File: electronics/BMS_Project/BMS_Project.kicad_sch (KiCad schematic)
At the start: 0 parts

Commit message: Meeting 28.04.2023 worked on schematic
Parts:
- added J1: Conn_01x20_Pin, symbol Connector:Conn_01x20_Pin
- added PAD1, PAD2: Prototyping_Pad_Data, BMS_lib:Prototyping_Pad_Data, symbol BMS_lib:Prototyping_Pad_Data
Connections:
- new net: J1.17 (Pin_17), PAD1.1
- new net: J1.18 (Pin_18), PAD2.1
- new net +5V: J1.2 (Pin_2)
- new net +BATT: J1.1 (Pin_1)
- new net GND: J1.19 (Pin_19), J1.20 (Pin_20)
- new net balancing_ctrl_1: J1.3 (Pin_3)
- new net balancing_ctrl_2: J1.4 (Pin_4)
- new net balancing_ctrl_3: J1.5 (Pin_5)
- new net balancing_ctrl_4: J1.6 (Pin_6)
- new net bat01: J1.7 (Pin_7)
- new net bat02: J1.8 (Pin_8)
- new net bat03: J1.9 (Pin_9)
- new net bat04: J1.10 (Pin_10)
- new net bat_main_switch: J1.15 (Pin_15)
- new net current_sensor: J1.16 (Pin_16)
- new net temp_sensor01: J1.11 (Pin_11)
- new net temp_sensor02: J1.12 (Pin_12)
- new net temp_sensor03: J1.13 (Pin_13)
- new net temp_sensor04: J1.14 (Pin_14)
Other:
- removed sheet Balancing
- sheet Arduino ports: added CAN_MISO, CAN_MOSI, CAN_SCK, balance_status_1, balance_status_2, balance_status_3, balance_status_4, bat_main_switch, cell_1_V, cell_2_V, cell_3_V, cell_4_V, current, temp_1, temp_2, temp_3, temp_4; removed none
- sheet Temp_sensor_circuit ports: added Temp_1, Temp_2, Temp_3, Temp_4, sensor_1, sensor_2, sensor_3, sensor_4; removed none
- sheet U_Messung ports: added BT1_+/BT2_-, BT2_+/BT3_-, BT3_+/BT4_-, BT4_+; removed BT1_+, BT1_-/BT2_+, BT2_-/BT3_+, BT3_-/BT4_+
- note removed: "Fabi"
- note removed: "John werte/values"
- note removed: "Michi"

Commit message: discord session with Johannes and Fabian, Schematic nearly done, all footprints fields filled
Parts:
- added F1: Fuse, Fuse:Fuse_1206_3216Metric, symbol Device:Fuse
- added J2, J6: Conn_01x01_Socket, Connector:Banana_Jack_1Pin, symbol Connector:Conn_01x01_Socket
- added J4: ESP32_power, TerminalBlock:TerminalBlock_bornier-2_P5.08mm, symbol Connector:Screw_Terminal_01x02
- added J5: Display_power, TerminalBlock:TerminalBlock_bornier-2_P5.08mm, symbol Connector:Screw_Terminal_01x02
- added Q1: Q_PMOS_GSD, Package_TO_SOT_SMD:SOT-23, symbol Device:Q_PMOS_GSD
- added SW2: SW_SPDT, Button_Switch_THT:SW_Slide_1P2T_CK_OS102011MS2Q, symbol Switch:SW_SPDT
- added U3: Buck, BMS_lib:Buck_LM2596, symbol BMS_lib:Buck_LM2596
- added U4: ~, BMS_lib:CAN_Board, symbol BMS_lib:CAN_board
- J1: footprint (none) -> Connector_IDC:IDC-Header_2x10_P2.54mm_Vertical
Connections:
- net +5V: now also F1.2, J4.1 (Pin_1), Q1.3 (D), U4.7 (VCC)
- net +BATT: now also SW2.3 (C)
- net GND: now also J2.1 (Pin_1), J4.2 (Pin_2), J5.2 (Pin_2), U3.2 (IN-), U3.4 (OUT-), U4.6 (GND)
- new net: SW2.2 (B), U3.1 (IN+)
- new net: F1.1, U3.3 (OUT+)
- new net: J5.1 (Pin_1), Q1.2 (S)
- new net: J6.1 (Pin_1), SW2.1 (A)
- new net CAN_SCK: U4.2 (SCK)
- new net CAN_SI: U4.3 (SI)
- new net CAN_SO: U4.4 (SO)
- new net display_enable: Q1.1 (G)
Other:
- sheet Arduino ports: added Display_enable; removed none
- note added: "?"
- note added: "Done: switch for power - via dcdc converter -> batt - via dcdc converter -> lab power supply one CAN module mosfet switch for display a few small buttons x4 fuse for logic voltage 5V output for ESP32 (mosfet switch -> no) banana sockets for aux power supply TODO: can pins ESP32 location?"
- moved on the sheet: J1, PAD1, PAD2

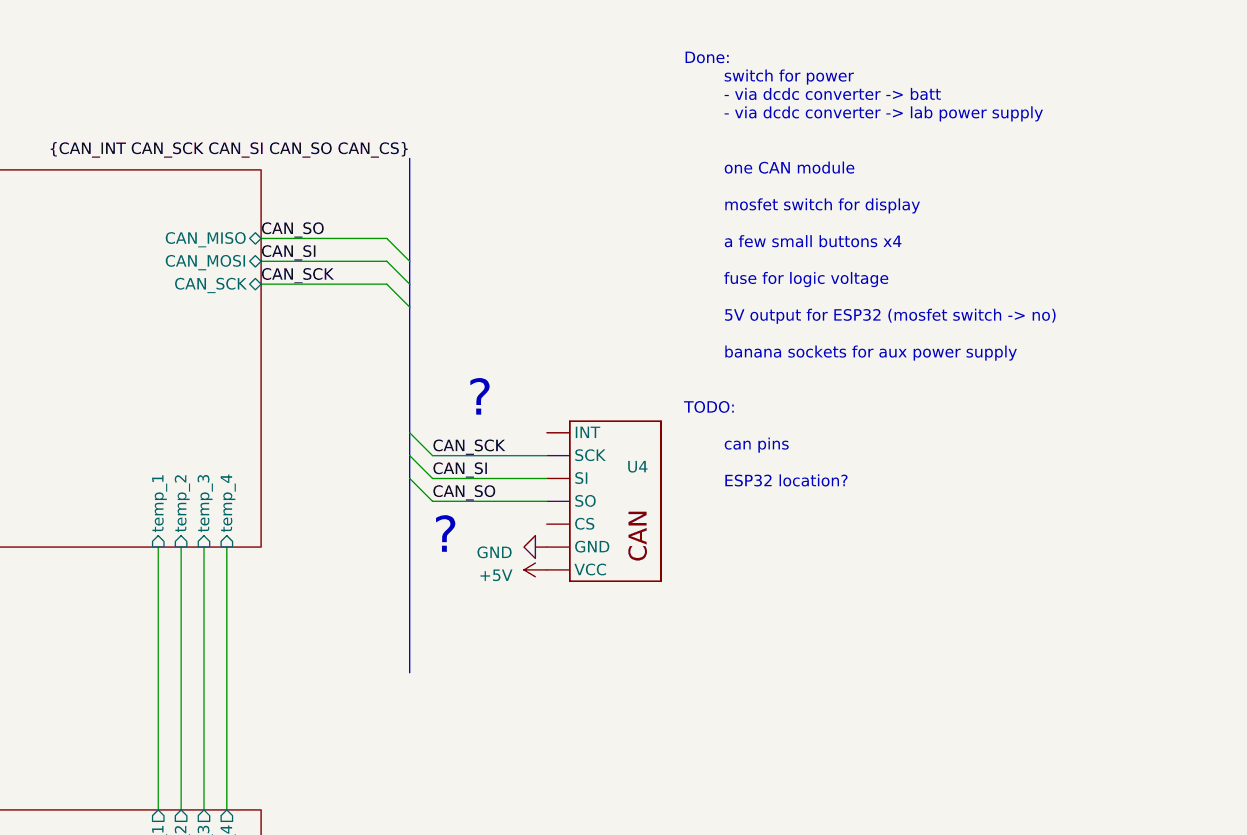
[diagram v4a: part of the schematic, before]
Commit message: schematic done, starting with layout
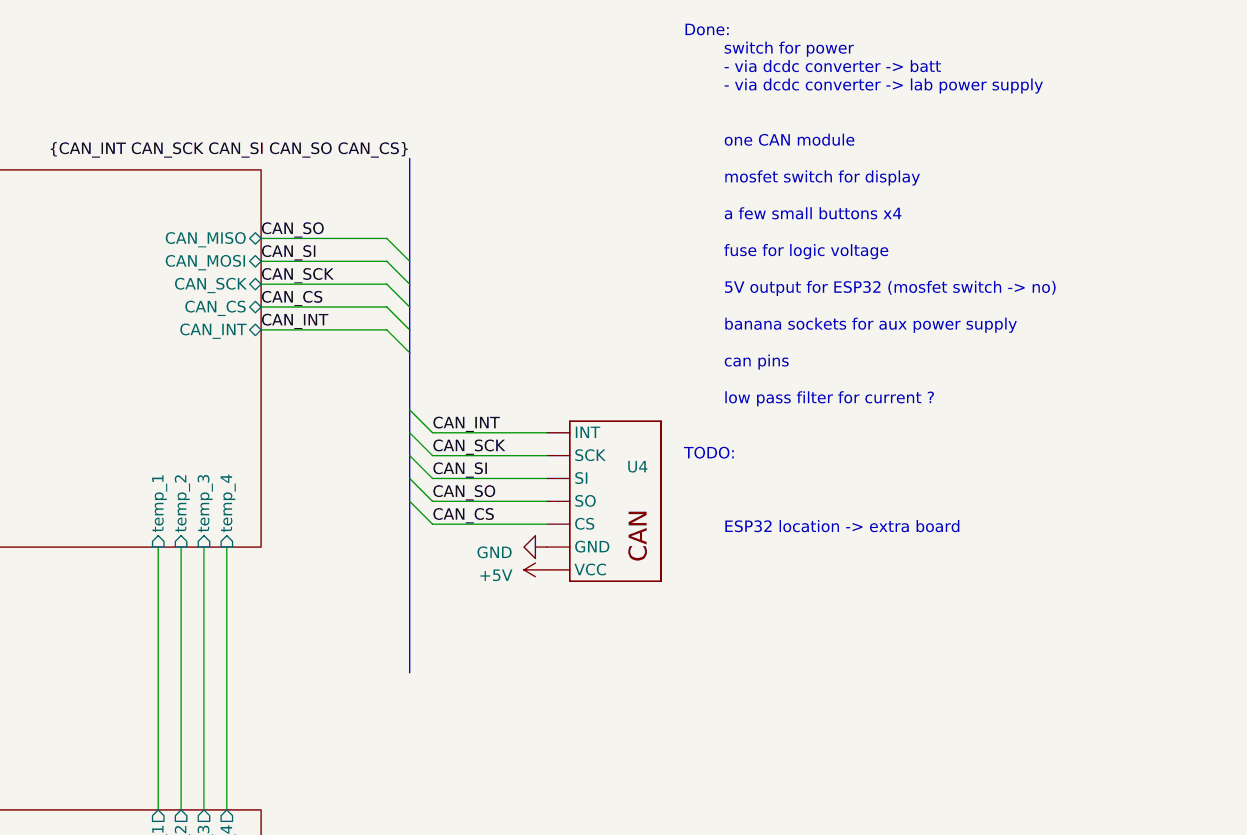
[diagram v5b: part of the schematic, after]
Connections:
- net CAN_INT: now reaches U4.1 (INT)
- net CAN_CS: now reaches U4.5 (CS)
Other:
- sheet Arduino ports: added CAN_CS, CAN_INT; removed none
- note added: "Done: switch for power - via dcdc converter -> batt - via dcdc converter -> lab power supply one CAN module mosfet switch for display a few small buttons x4 fuse for logic voltage 5V output for ESP32 (mosfet switch -> no) banana sockets for aux power supply can pins low pass filter for current ? TODO: ESP32 location -> extra board"
- note removed: "?"
- note removed: "Done: switch for power - via dcdc converter -> batt - via dcdc converter -> lab power supply one CAN module mosfet switch for display a few small buttons x4 fuse for logic voltage 5V output for ESP32 (mosfet switch -> no) banana sockets for aux power supply TODO: can pins ESP32 location?"
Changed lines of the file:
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@@
+    (stroke (width 0) (type default))
+  )
+  (bus_entry (at 201.93 45.72) (size -2.54 -2.54)
     (stroke (width 0) (type default))
   )
@@
     (stroke (width 0) (type default))
   )
+  (bus_entry (at 201.93 48.26) (size -2.54 -2.54)
+    (stroke (width 0) (type default))
+  )
   (bus_entry (at 114.3 115.57) (size 2.54 -2.54)
     (stroke (width 0) (type default))
   )
+  (bus_entry (at 201.93 54.61) (size 2.54 2.54)
+    (stroke (width 0) (type default))
+  )
   (bus_entry (at 114.3 53.34) (size 2.54 -2.54)
     (stroke (width 0) (type default))
@@
     (stroke (width 0) (type default))
   )
+  (bus_entry (at 201.93 64.77) (size 2.54 2.54)
+    (stroke (width 0) (type default))
+  )
   (bus_entry (at 114.3 113.03) (size 2.54 -2.54)
     (stroke (width 0) (type default))
@@
     (stroke (width 0) (type default))
   )
+  (wire (pts (xy 204.47 67.31) (xy 217.17 67.31))
+    (stroke (width 0) (type default))
+  )
   (wire (pts (xy 116.84 53.34) (xy 134.62 53.34))
     (stroke (width 0) (type default))
@@
     (stroke (width 0) (type default))
   )
-  (bus (pts (xy 201.93 43.18) (xy 201.93 57.15))
+  (bus (pts (xy 201.93 43.18) (xy 201.93 45.72))
     (stroke (width 0) (type default))
   )
@@
     (stroke (width 0) (type default))
   )
+  (bus (pts (xy 201.93 54.61) (xy 201.93 57.15))
+    (stroke (width 0) (type default))
+  )
+  (bus (pts (xy 201.93 48.26) (xy 201.93 54.61))
+    (stroke (width 0) (type default))
+  )
   (wire (pts (xy 57.15 180.34) (xy 57.15 181.61))
     (stroke (width 0) (type default))
@@
     (stroke (width 0) (type default))
   )
+  (bus (pts (xy 201.93 45.72) (xy 201.93 48.26))
+    (stroke (width 0) (type default))
+  )
   (bus (pts (xy 201.93 26.67) (xy 201.93 38.1))
     (stroke (width 0) (type default))
@@
     (stroke (width 0) (type default))
   )
-  (bus (pts (xy 201.93 62.23) (xy 201.93 83.82))
+  (bus (pts (xy 201.93 62.23) (xy 201.93 64.77))
+    (stroke (width 0) (type default))
+  )
+  (wire (pts (xy 204.47 57.15) (xy 217.17 57.15))
     (stroke (width 0) (type default))
   )
@@
     (stroke (width 0) (type default))
   )
+  (bus (pts (xy 201.93 64.77) (xy 201.93 83.82))
+    (stroke (width 0) (type default))
+  )
   (wire (pts (xy 30.48 123.19) (xy 50.8 123.19))
     (stroke (width 0) (type default))
@@
     (stroke (width 0) (type default))
   )
+  (wire (pts (xy 185.42 45.72) (xy 199.39 45.72))
+    (stroke (width 0) (type default))
+  )
   (wire (pts (xy 77.47 35.56) (xy 134.62 35.56))
     (stroke (width 0) (type default))
@@
     (stroke (width 0) (type default))
   )
+  (wire (pts (xy 185.42 43.18) (xy 199.39 43.18))
+    (stroke (width 0) (type default))
+  )
   (bus (pts (xy 53.34 120.65) (xy 53.34 123.19))
     (stroke (width 0) (type default))
@@
     (stroke (width 0) (type default))
   )
-  (text "Done:\n		switch for power\n		- via dcdc converter -> batt\n		- via dcdc converter -> lab power supply\n\n\n		one CAN module\n\n		mosfet switch for display\n\n		a few small buttons x4\n\n		fuse for logic voltage\n\n		5V output for ESP32 (mosfet switch -> no)\n\n		banana sockets for aux power supply\n\n\nTODO:\n\n		can pins\n\n		ESP32 location?"
-    (at 232.41 63.5 0)
+  (text "Done:\n		switch for power\n		- via dcdc converter -> batt\n		- via dcdc converter -> lab power supply\n\n\n		one CAN module\n\n		mosfet switch for display\n\n		a few small buttons x4\n\n		fuse for logic voltage\n\n		5V output for ESP32 (mosfet switch -> no)\n\n		banana sockets for aux power supply\n\n		can pins\n\n		low pass filter for current ?\n\n\nTODO:\n\n\n\n		ESP32 location -> extra board\n"
+    (at 232.41 68.58 0)
     (effects (font (size 1.27 1.27)) (justify left bottom))
   )
   (text "GND and +12V\nvia global labels" (at 60.96 25.4 0)
     (effects (font (size 1.27 1.27)) (justify left bottom))
-  )
-  (text "?" (at 208.28 55.88 0)
-    (effects (font (size 4 4)) (justify left bottom))
-  )
-  (text "?" (at 204.47 71.12 0)
-    (effects (font (size 4 4)) (justify left bottom))
   )
   (label "bat_main_switch" (at 30.48 128.27 0) (fields_autoplaced)
@@
     (effects (font (size 1.27 1.27)) (justify left bottom))
   )
+  (label "CAN_CS" (at 185.42 43.18 0)
+    (effects (font (size 1.27 1.27)) (justify left bottom))
+  )
   (label "bat03" (at 30.48 113.03 0) (fields_autoplaced)
     (effects (font (size 1.27 1.27)) (justify left bottom))
@@
     (effects (font (size 1.27 1.27)) (justify left bottom))
   )
+  (label "CAN_INT" (at 204.47 57.15 0)
+    (effects (font (size 1.27 1.27)) (justify left bottom))
+  )
   (label "temp_sensor02" (at 116.84 110.49 0) (fields_autoplaced)
     (effects (font (size 1.27 1.27)) (justify left bottom))
@@
   )
   (label "CAN_SI" (at 185.42 38.1 0) (fields_autoplaced)
+    (effects (font (size 1.27 1.27)) (justify left bottom))
+  )
+  (label "CAN_CS" (at 204.47 67.31 0)
+    (effects (font (size 1.27 1.27)) (justify left bottom))
+  )
+  (label "CAN_INT" (at 185.42 45.72 0)
     (effects (font (size 1.27 1.27)) (justify left bottom))
   )
@@
       (effects (font (size 1.27 1.27)) (justify left))
     )
-    (instances
+    (pin "CAN_CS" bidirectional (at 185.42 43.18 0)
+      (effects (font (size 1.27 1.27)) (justify right))
+    )
+    (pin "CAN_INT" bidirectional (at 185.42 45.72 0)
+      (effects (font (size 1.27 1.27)) (justify right))
+    )
+    (instances

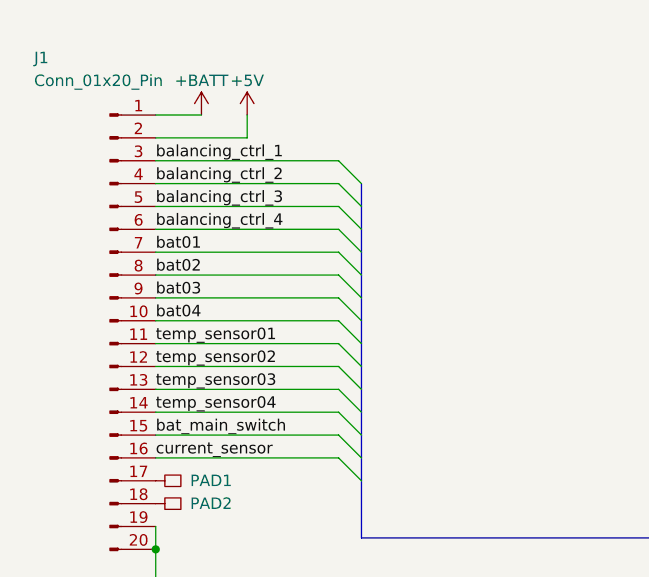
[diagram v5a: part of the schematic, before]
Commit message: Started PCB layout and adjusted schematic to suit the layout needs better
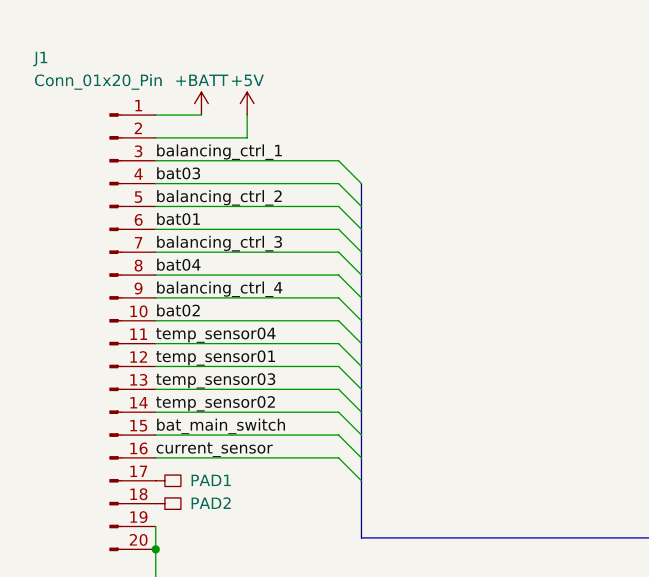
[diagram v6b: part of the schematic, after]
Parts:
- PAD1: value Prototyping_Pad_Data -> Pin_17
- PAD2: value Prototyping_Pad_Data -> Pin_18
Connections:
- net balancing_ctrl_2: now also J1.5 (Pin_5); no longer J1.4 (Pin_4)
- net balancing_ctrl_3: now also J1.7 (Pin_7); no longer J1.5 (Pin_5)
- net balancing_ctrl_4: now also J1.9 (Pin_9); no longer J1.6 (Pin_6)
- net bat01: now also J1.6 (Pin_6); no longer J1.7 (Pin_7)
- net bat02: now also J1.10 (Pin_10); no longer J1.8 (Pin_8)
- net bat03: now also J1.4 (Pin_4); no longer J1.9 (Pin_9)
- net bat04: now also J1.8 (Pin_8); no longer J1.10 (Pin_10)
- net temp_sensor01: now also J1.12 (Pin_12); no longer J1.11 (Pin_11)
- net temp_sensor02: now also J1.14 (Pin_14); no longer J1.12 (Pin_12)
- net temp_sensor04: now also J1.11 (Pin_11); no longer J1.14 (Pin_14)
